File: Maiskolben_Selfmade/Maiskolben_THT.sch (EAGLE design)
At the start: 33 parts, among them IC1 OPA703PA, J2 AUDIO_JACK_5PEBS_35, Q1 IRF5305, Q2 2N7000, U1 CD4050DIP16, U2 ARDUINO_NANOR3

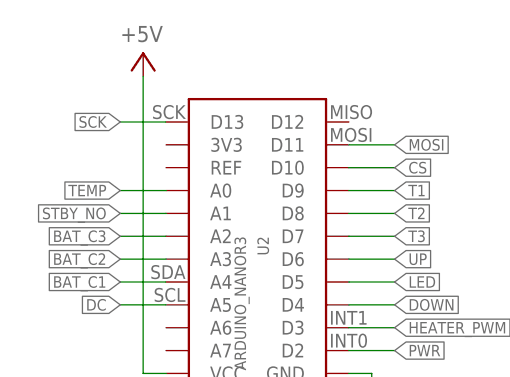
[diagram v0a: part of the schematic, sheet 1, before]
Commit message: Fixed 3v3 connection
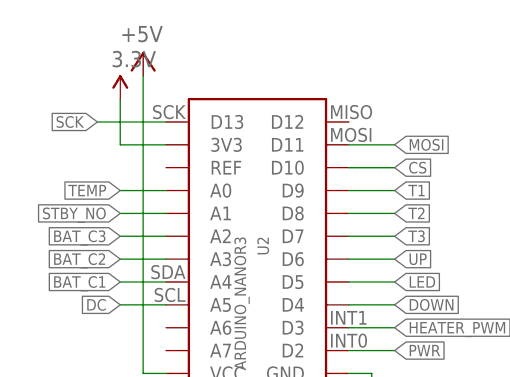
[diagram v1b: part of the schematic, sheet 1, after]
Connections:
- net 3.3V: now also U2.3V3
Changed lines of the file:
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@@
 <attributes>
 <attribute name="CNAME" value="Maiskolben THT"/>
-<attribute name="CREVISION" value="1.0"/>
+<attribute name="CREVISION" value="1.1"/>
 <attribute name="DESIGNER" value="Luca Zimmermann"/>
 </attributes>
@@
 <part name="R14" library="SparkFun-Resistors" deviceset="RESISTOR" device="AXIAL-0.3" value="0R"/>
 <part name="U$1" library="rgb_matrix" deviceset="HANNIO" device="_MEDIUM"/>
+<part name="SUPPLY2" library="SparkFun-Aesthetics" deviceset="3.3V" device=""/>
 </parts>
 <sheets>
@@
 <instance part="R14" gate="G$1" x="76.2" y="170.18" rot="R180"/>
 <instance part="U$1" gate="G$1" x="226.06" y="15.24"/>
+<instance part="SUPPLY2" gate="G$1" x="7.62" y="170.18"/>
 </instances>
 <busses>
@@
 <segment>
 <pinref part="U2" gate="G$1" pin="D13"/>
-<wire x1="12.7" y1="167.64" x2="7.62" y2="167.64" width="0.1524" layer="91"/>
-<label x="7.62" y="167.64" size="1.27" layer="95" rot="R180" xref="yes"/>
+<wire x1="12.7" y1="167.64" x2="5.08" y2="167.64" width="0.1524" layer="91"/>
+<label x="5.08" y="167.64" size="1.27" layer="95" rot="R180" xref="yes"/>
 </segment>
 </net>
@@
 <junction x="104.14" y="104.14"/>
 </segment>
-</net>
+<segment>
+<pinref part="U2" gate="G$1" pin="3V3"/>
+<pinref part="SUPPLY2" gate="G$1" pin="3.3V"/>
+<wire x1="12.7" y1="165.1" x2="7.62" y2="165.1" width="0.1524" layer="91"/>
+<wire x1="7.62" y1="165.1" x2="7.62" y2="170.18" width="0.1524" layer="91"/>
+</segment>
+</net>

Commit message: Push to HW V1.3
Closes #3, adds drill file (whoops), adds optional LM7805 for v > 12V
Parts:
- added IC2: 7805TV, linear:7805TV
- added R6: 100K, SparkFun-Resistors:RESISTORAXIAL-0.3
- added SJ1: DIRECT VIN, SparkFun-Passives:JUMPER-PAD-2-NOYES_SILK
- R2, R8: value 5K6 -> 5k6
- R4: value 68K -> 68k
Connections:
- new net A_VIN: SJ1.1, U2.VIN
- net +5V: now also IC2.VO
- net DGND: now also IC2.GND, R6.1
- net OPA+: now also R6.2
- net VIN: now also IC2.VI, SJ1.2; no longer U2.VIN
